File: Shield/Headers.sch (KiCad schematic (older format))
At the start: 12 parts, among them J1 EXPANSION, J10 E0 MOT/STOP, J11 E0 HEAT/TEMP/FAN, J20 5V_PS, J23 POWER IN, J24 GND V_IN, J28 Probe, J4 BED HEATER, J5 BED TEMP, J7 Z MOT/STOP, J8 Y MOT/STOP, J9 X MOT/STOP

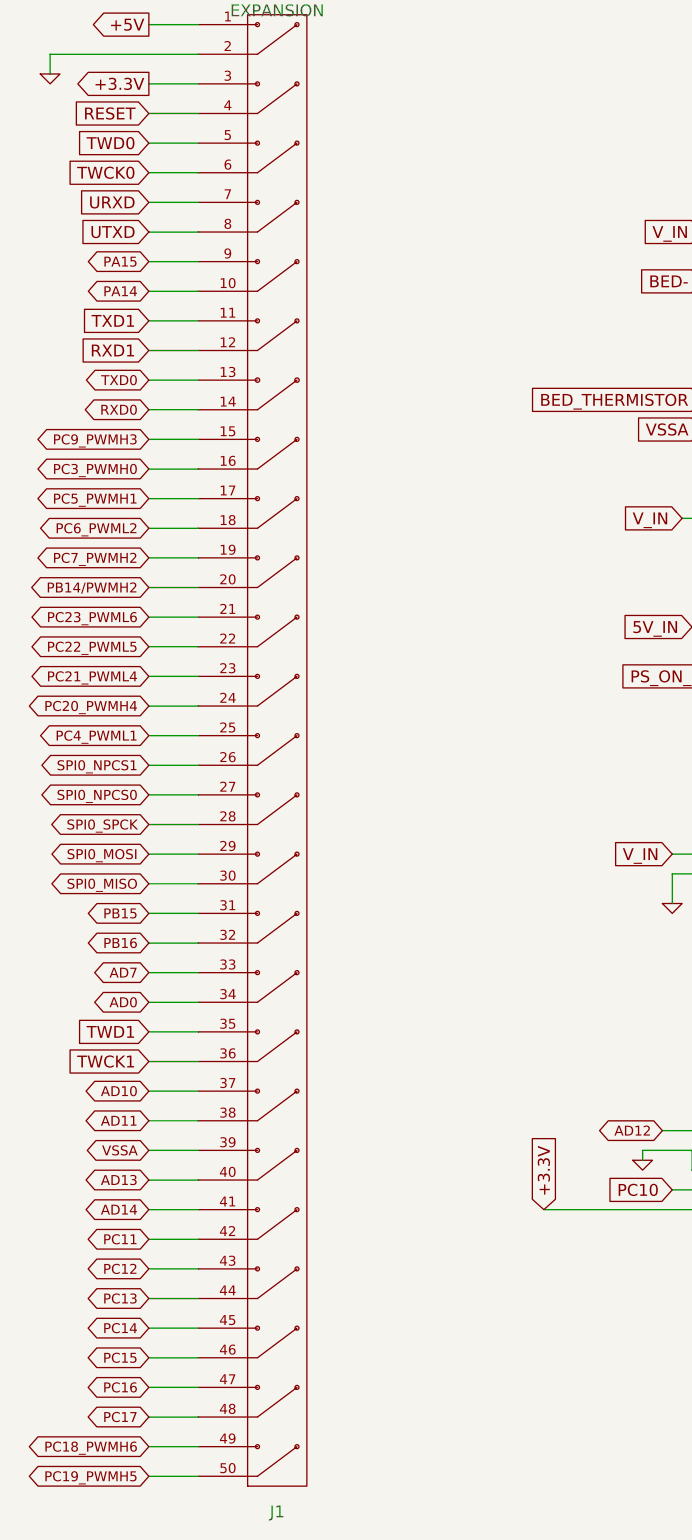
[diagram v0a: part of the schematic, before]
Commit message: All schematic connections to the stepper drivers, heaters, and thermistors complete.
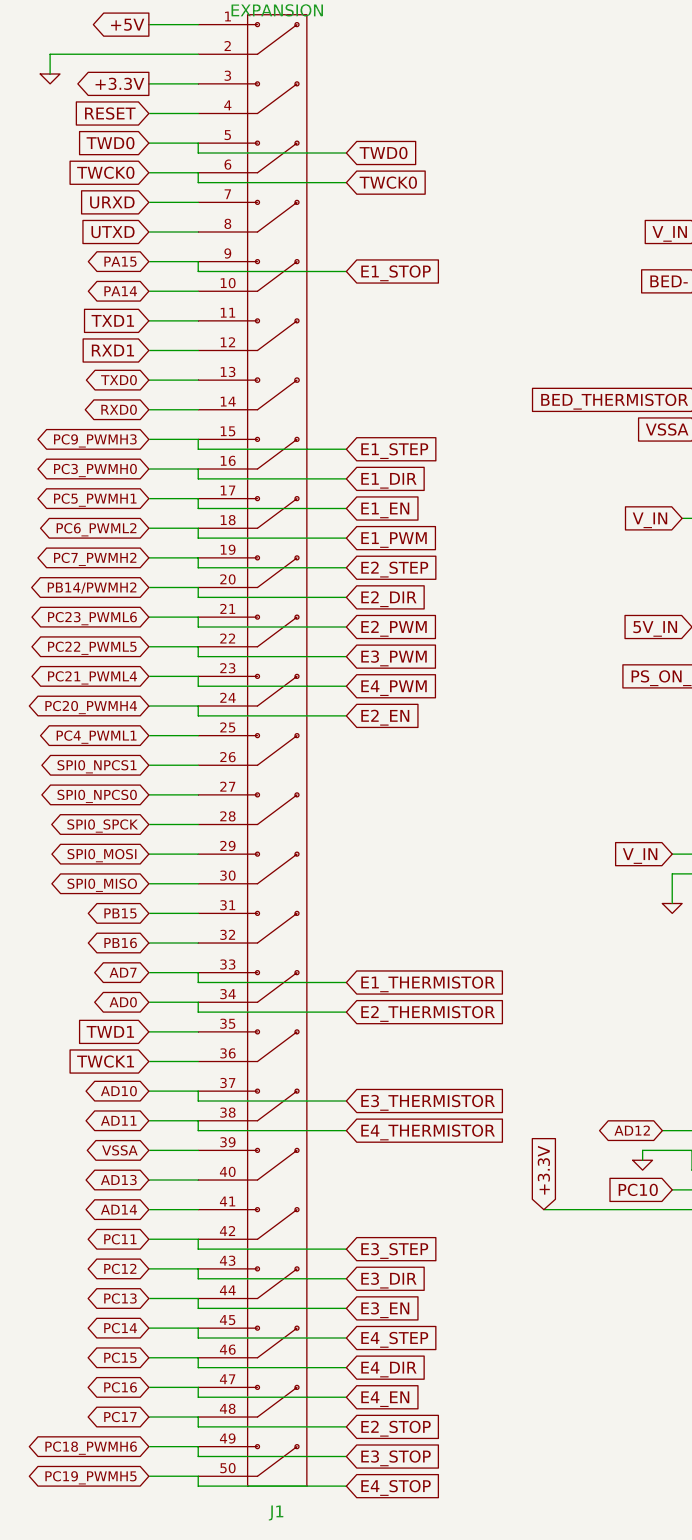
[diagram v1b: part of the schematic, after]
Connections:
- net PA15 renamed E1_STOP
- net PB14/PWMH2 renamed E2_DIR
- net PC11 renamed E3_STEP
- net PC12 renamed E3_DIR
- net PC13 renamed E3_EN
- net PC14 renamed E4_STEP
- net PC15 renamed E4_DIR
- net PC16 renamed E4_EN
- net PC17 renamed E2_STOP
- net PC18_PWMH6 renamed E3_STOP
- net PC19_PWMH5 renamed E4_STOP
- net PC20_PWMH4 renamed E2_EN
- net PC21_PWML4 renamed E4_PWM
- net PC22_PWML5 renamed E3_PWM
- net PC23_PWML6 renamed E2_PWM
- net PC3_PWMH0 renamed E1_DIR
- net PC5_PWMH1 renamed E1_EN
- net PC6_PWML2 renamed E1_PWM
- net PC7_PWMH2 renamed E2_STEP
- net PC9_PWMH3 renamed E1_STEP
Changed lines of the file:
@@
-EESchema Schematic File Version 2  date 19/07/2014 15:49:20
+EESchema Schematic File Version 2  date Thu 06 Nov 2014 10:06:04 GMT
 LIBS:power
 LIBS:device
@@
 LIBS:valves
 LIBS:FE
-LIBS:Duet0.7-cache
+LIBS:Shield-cache
 EELAYER 25  0
 EELAYER END
@@
 Sheet 4 7
 Title "Duet"
-Date "19 jul 2014"
+Date "5 nov 2014"
 Rev "0.7"
 Comp "Think3DPrint3D, RepRapPro"
@@
 Comment4 ""
 $EndDescr
+Text GLabel 2600 1500 2    60   Input ~ 0
+TWCK0
+Text GLabel 2600 1350 2    60   Input ~ 0
+TWD0
+Wire Wire Line
+	2600 1500 1850 1500
+Wire Wire Line
+	1850 1500 1850 1450
+Wire Wire Line
+	2600 8100 1850 8100
+Wire Wire Line
+	1850 8100 1850 8050
+Wire Wire Line
+	2600 7800 1850 7800
+Wire Wire Line
+	1850 7800 1850 7750
+Wire Wire Line
+	2600 7500 1850 7500
+Wire Wire Line
+	1850 7500 1850 7450
+Wire Wire Line
+	2600 7200 1850 7200
+Wire Wire Line
+	1850 7200 1850 7150
+Wire Wire Line
+	2600 6900 1850 6900
+Wire Wire Line
+	1850 6900 1850 6850
+Wire Wire Line
+	2600 6150 1850 6150
+Wire Wire Line
+	1850 6150 1850 6100
+Wire Wire Line
+	2600 5550 1850 5550
+Wire Wire Line
+	1850 5550 1850 5500
+Wire Wire Line
+	2600 3900 1850 3900
+Wire Wire Line
+	1850 3900 1850 3850
+Wire Wire Line
+	2600 3600 1850 3600
+Wire Wire Line
+	1850 3600 1850 3550
+Wire Wire Line
+	2600 3300 1850 3300
+Wire Wire Line
+	1850 3300 1850 3250
+Wire Wire Line
+	2600 3000 1850 3000
+Wire Wire Line
+	1850 3000 1850 2950
+Wire Wire Line
+	2600 2850 1850 2850
+Wire Wire Line
+	1850 2850 1850 2800
 Wire Wire Line
 	9450 6350 9450 6500
@@
 	4450 3300 4650 3300
 Wire Wire Line
-	1850 1900 1600 1900
+	1600 1900 1850 1900
 Wire Wire Line
 	1850 1600 1600 1600
 Wire Wire Line
-	1850 1300 1600 1300
+	1600 1300 1850 1300
 Wire Wire Line
 	1600 1000 1850 1000
 Wire Wire Line
-	1850 5650 1600 5650
+	1600 5650 1850 5650
 Wire Wire Line
 	1600 7900 1850 7900
 Wire Wire Line
-	1600 6100 1850 6100
+	1850 6100 1600 6100
 Wire Wire Line
 	1600 5800 1850 5800
@@
 	1850 3850 1600 3850
 Wire Wire Line
-	1600 3550 1850 3550
-Wire Wire Line
-	1600 3250 1850 3250
-Wire Wire Line
-	1600 2950 1850 2950
+	1850 3550 1600 3550
+Wire Wire Line
+	1850 3250 1600 3250
+Wire Wire Line
+	1850 2950 1600 2950
 Wire Wire Line
 	1600 2650 1850 2650
@@
 	1600 2350 1850 2350
 Wire Wire Line
-	1600 2800 1850 2800
+	1850 2800 1600 2800
 Wire Wire Line
 	1600 3100 1850 3100
@@
 	1600 5200 1850 5200
 Wire Wire Line
-	1600 5500 1850 5500
+	1850 5500 1600 5500
 Wire Wire Line
 	1850 5950 1600 5950
@@
 	1600 6250 1850 6250
 Wire Wire Line
-	1600 8050 1850 8050
+	1850 8050 1600 8050
 Wire Wire Line
 	1600 2500 1850 2500
@@
 	1850 2050 1600 2050
 Wire Wire Line
-	1600 7750 1850 7750
+	1850 7750 1600 7750
 Wire Wire Line
 	1850 7450 1600 7450
@@
 	1600 6550 1850 6550
 Wire Wire Line
-	1600 6850 1850 6850
+	1850 6850 1600 6850
 Wire Wire Line
 	1600 7300 1850 7300
@@
 Wire Wire Line
 	9350 6250 9450 6250
+Wire Wire Line
+	1850 1900 1850 1950
+Wire Wire Line
+	1850 1950 2600 1950
+Wire Wire Line
+	1850 4150 1850 4200
+Wire Wire Line
+	1850 4200 2600 4200
+Wire Wire Line
+	1850 3100 1850 3150
+Wire Wire Line
+	1850 3150 2600 3150
+Wire Wire Line
+	1850 3400 1850 3450
+Wire Wire Line
+	1850 3450 2600 3450
+Wire Wire Line
+	1850 3700 1850 3750
+Wire Wire Line
+	1850 3750 2600 3750
+Wire Wire Line
+	1850 4000 1850 4050
+Wire Wire Line
+	1850 4050 2600 4050
+Wire Wire Line
+	1850 5650 1850 5700
+Wire Wire Line
+	1850 5700 2600 5700
+Wire Wire Line
+	1850 6250 1850 6300
+Wire Wire Line
+	1850 6300 2600 6300
+Wire Wire Line
+	1850 7000 1850 7050
+Wire Wire Line
+	1850 7050 2600 7050
+Wire Wire Line
+	1850 7300 1850 7350
+Wire Wire Line
+	1850 7350 2600 7350
+Wire Wire Line
+	1850 7600 1850 7650
+Wire Wire Line
+	1850 7650 2600 7650
+Wire Wire Line
+	1850 7900 1850 7950
+Wire Wire Line
+	1850 7950 2600 7950
+Wire Wire Line
+	1850 1300 1850 1350
+Wire Wire Line
+	1850 1350 2600 1350
+Text GLabel 2600 8100 2    60   Input ~ 0
+E4_STOP
+Text GLabel 2600 7950 2    60   Input ~ 0
+E3_STOP
+Text GLabel 2600 7800 2    60   Input ~ 0
+E2_STOP
+Text GLabel 2600 7650 2    60   Input ~ 0
+E4_EN
+Text GLabel 2600 7500 2    60   Input ~ 0
+E4_DIR
+Text GLabel 2600 7350 2    60   Input ~ 0
+E4_STEP
+Text GLabel 2600 7200 2    60   Input ~ 0
+E3_EN
+Text GLabel 2600 7050 2    60   Input ~ 0
+E3_DIR
+Text GLabel 2600 6900 2    60   Input ~ 0
+E3_STEP
+Text GLabel 2600 6300 2    60   Input ~ 0
+E4_THERMISTOR
+Text GLabel 2600 6150 2    60   Input ~ 0
+E3_THERMISTOR
+Text GLabel 2600 5700 2    60   Input ~ 0
+E2_THERMISTOR
+Text GLabel 2600 5550 2    60   Input ~ 0
+E1_THERMISTOR
+Text GLabel 2600 4200 2    60   Input ~ 0
+E2_EN
+Text GLabel 2600 4050 2    60   Input ~ 0
+E4_PWM
+Text GLabel 2600 3900 2    60   Input ~ 0
+E3_PWM
+Text GLabel 2600 3750 2    60   Input ~ 0
+E2_PWM
+Text GLabel 2600 3600 2    60   Input ~ 0
+E2_DIR
+Text GLabel 2600 3450 2    60   Input ~ 0
+E2_STEP
+Text GLabel 2600 3300 2    60   Input ~ 0
+E1_PWM
+Text GLabel 2600 3150 2    60   Input ~ 0
+E1_EN
+Text GLabel 2600 3000 2    60   Input ~ 0
+E1_DIR
+Text GLabel 2600 2850 2    60   Input ~ 0
+E1_STEP
+Text GLabel 2600 1950 2    60   Input ~ 0
+E1_STOP
 $Comp
 L CONN_10 J11

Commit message: About 75% of the schematic changes made.
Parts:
- added J? (x2): E0 HEAT/TEMP/FAN, symbol CONN_10
- added J? (x2): E0 MOT/STOP, symbol CONN7
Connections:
- net BED_THERMISTOR is gone; now on net AD7: J5.2 (PM)
- net PC10 is gone; now on net AD14: J28.3 (P3)
- net +3.3V: now also J?.6 (P6)
- net AD12: now also J1.39
- net AD7: now also J11.5 (P5)
- net E0-: now also J?.1 (P1), J?.1 (P1), J?.2 (P2), J?.2 (P2); no longer J11.1 (P1), J11.2 (P2)
- net E0_MOT_1A: now also J?.2 (P2), J?.2 (P2); no longer J10.2 (P2)
- net E0_MOT_1B: now also J?.1 (P1), J?.1 (P1); no longer J10.1 (P1)
- net E0_MOT_2A: now also J?.3 (P3), J?.3 (P3); no longer J10.3 (P3)
- net E0_MOT_2B: now also J?.4 (P4), J?.4 (P4); no longer J10.4 (P4)
- net E0_STOP_CONN: now also J?.5 (P5), J?.5 (P5); no longer J10.5 (P5)
- net E0_THERMISTOR: now also J?.5 (P5), J?.5 (P5); no longer J11.5 (P5)
- net FAN0-: now also J?.9 (P9), J?.9 (P9)
- net GND: now also J?.7 (P7), J?.7 (P7), J?.8 (P8), J?.8 (P8)
- net VSSA: now also J?.6 (P6), J?.6 (P6); no longer J1.39
- net V_IN: now also J?.10 (P10), J?.10 (P10), J?.3 (P3), J?.3 (P3), J?.4 (P4), J?.4 (P4), J?.7 (P7), J?.7 (P7)
- net BED- renamed E1-
- net E1-: now also J11.1 (P1), J11.2 (P2)
- net E1_STOP renamed CTS1
- net PA14 renamed RTS1
- net X_MOT_1A renamed E1_MOT_1A
- net X_MOT_1B renamed E1_MOT_1B
- net X_MOT_2A renamed E1_MOT_2A
- net X_MOT_2B renamed E1_MOT_2B
- net X_STOP_CONN renamed E1_STOP_CONN
- net Y_MOT_1A renamed E2_MOT_1A
- net Y_MOT_1B renamed E2_MOT_1B
- net Y_MOT_2A renamed E2_MOT_2A
- net Y_MOT_2B renamed E2_MOT_2B
- net Y_STOP_CONN renamed E2_STOP_CONN
- net Z_MOT_1A renamed E3_MOT_1A
- net Z_MOT_1B renamed E3_MOT_1B
- net Z_MOT_2A renamed E3_MOT_2A
- net Z_MOT_2B renamed E3_MOT_2B
- net Z_STOP_CONN renamed E3_STOP_CONN
- new net E4_MOT_1A: J10.2 (P2)
- new net E4_MOT_1B: J10.1 (P1)
- new net E4_MOT_2A: J10.3 (P3)
- new net E4_MOT_2B: J10.4 (P4)
- new net E4_STOP_CONN: J10.5 (P5)
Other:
- note added: "Change to 6 pin"
- note added: "Feedthrough"
- note added: "spade connectors"

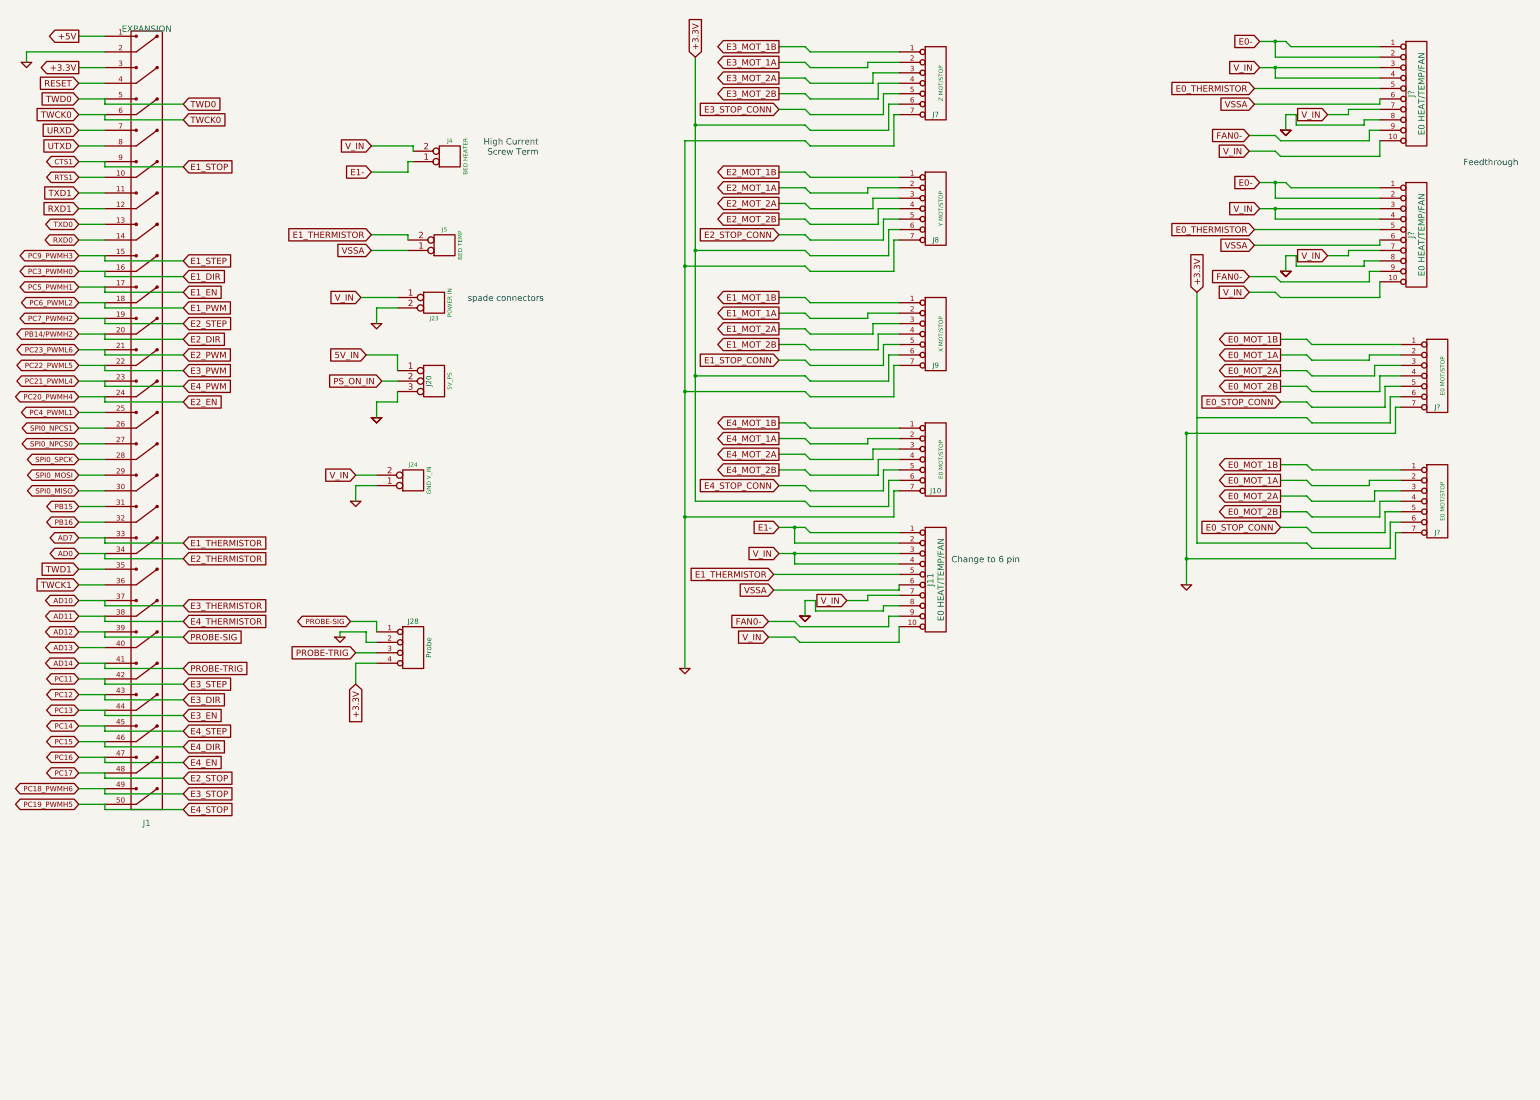
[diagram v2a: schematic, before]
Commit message: First hack at the shield schematic.
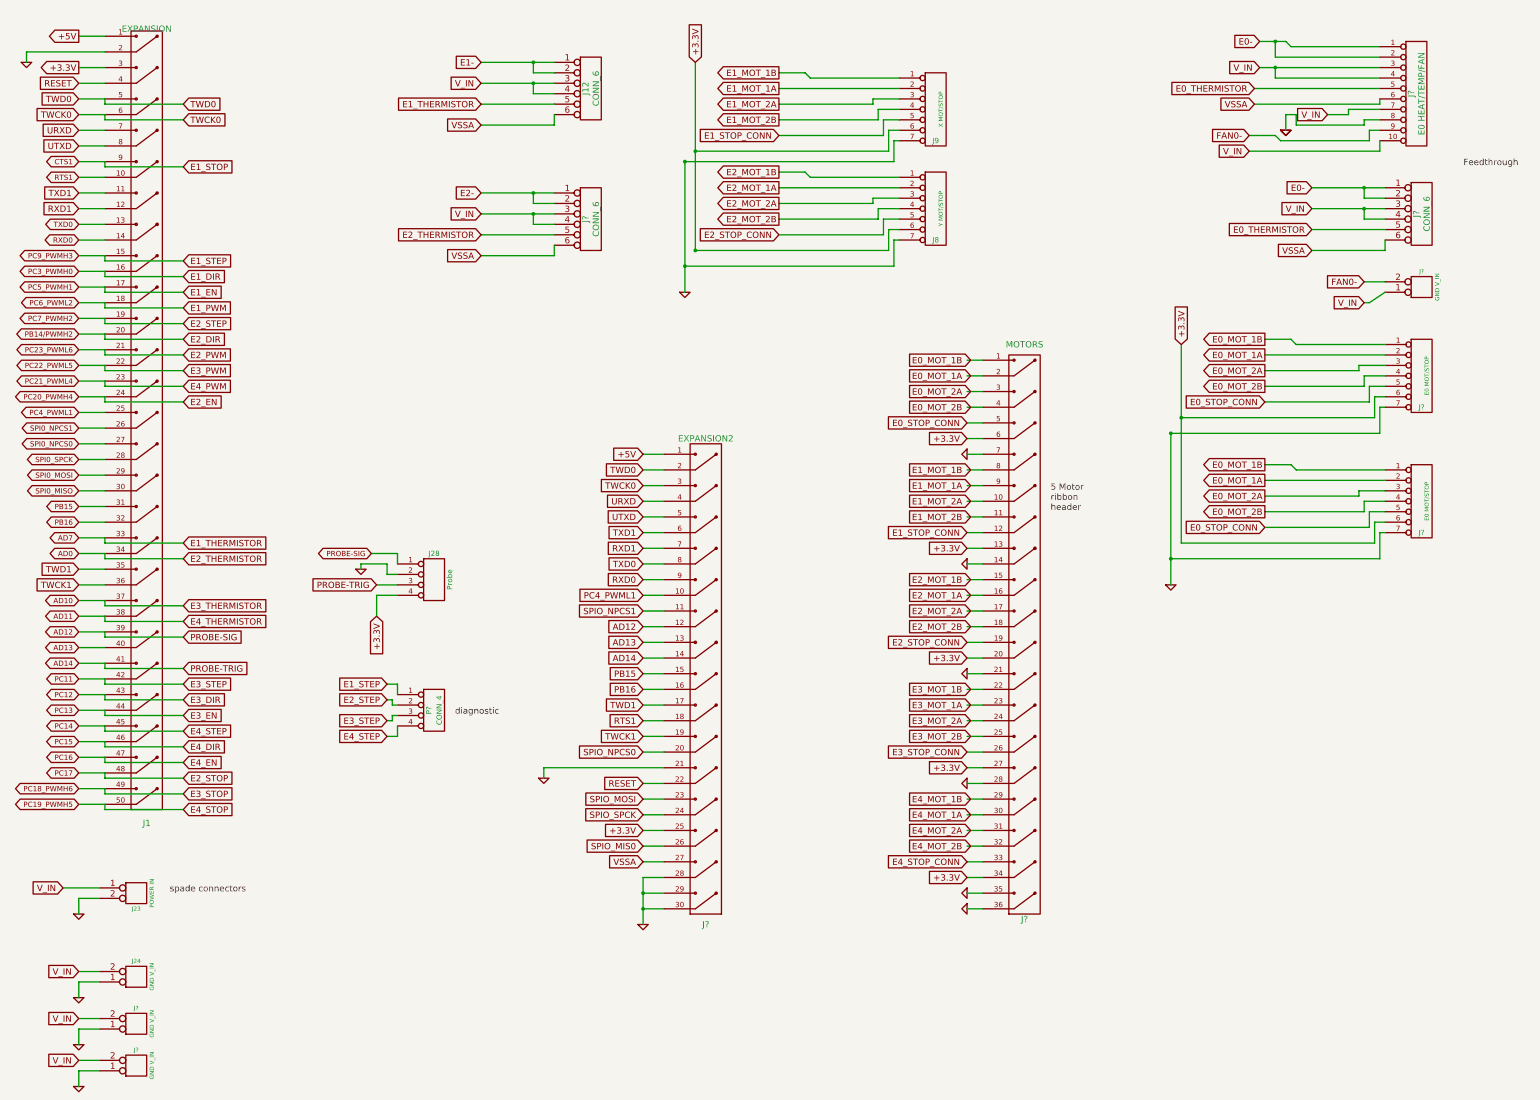
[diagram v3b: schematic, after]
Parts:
- removed J10: E0 MOT/STOP, symbol CONN7
- removed J11, J?: E0 HEAT/TEMP/FAN, symbol CONN_10
- removed J20: 5V_PS, symbol CONN_3
- removed J4: BED HEATER, symbol CONN2
- removed J5: BED TEMP, symbol CONN2
- removed J7: Z MOT/STOP, symbol CONN7
- added J12, J? (x2): CONN_6, symbol CONN_6
- added J? (x3): GND V_IN, symbol CONN2
- added J?: MOTORS, symbol CONN2X18
- added J?: EXPANSION2, symbol CONN2X15
- added P?: CONN_4, symbol CONN_4
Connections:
- net labels added: E2-, SPIO_MIS0, SPIO_MOSI, SPIO_NPCS0, SPIO_NPCS1, SPIO_SPCK
- net labels removed: 5V_IN, PS_ON_IN
- wire segments 419 -> 357
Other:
- note added: "5 Motor\nribbon\nheader"
- note added: "diagnostic"
- note removed: "Change to 6 pin"
- note removed: "High Current\nScrew Term"
- moved on the sheet: J23, J24, J28, J9, J?
